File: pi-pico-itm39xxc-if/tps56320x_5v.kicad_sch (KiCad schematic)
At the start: 16 parts

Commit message: Working on pico itm interface
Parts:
- R?: value 30k -> 11k
- R?: value 9k1 -> 2k
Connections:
- net 3V3 renamed 5V
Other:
- note added: "Supply info - Input voltage: 6.7 V - 17 V - Output voltage: 5 V - Output current: 3 A Compatible switching regulators: - TPS56320x - TPS56220x TODO - Make feedback resistors, output capacitors and inductor configurable from the sheet, so that it is possible to obtain any output voltage without changing values inside the sheet."
- note removed: "Supply info - Input voltage: 4.5 V - 17 V - Output voltage: 3.3 V - Output current: 3 A Compatible switching regulators: - TPS56320x - TPS56220x TODO - Make feedback resistors, output capacitors and inductor configurable from the sheet, so that it is possible to obtain any output voltage without changing values inside the sheet."
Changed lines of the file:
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@@
     (stroke (width 0) (type default) (color 0 0 0 0))
   )
-  (text "Supply info\n - Input voltage: 4.5 V - 17 V\n - Output voltage: 3.3 V\n - Output current: 3 A\n\nCompatible switching regulators:\n - TPS56320x\n - TPS56220x\n\nTODO\n - Make feedback resistors, output capacitors and inductor \n configurable from the sheet, so that it is possible to obtain\n any output voltage without changing values inside the sheet."
+  (text "Supply info\n - Input voltage: 6.7 V - 17 V\n - Output voltage: 5 V\n - Output current: 3 A\n\nCompatible switching regulators:\n - TPS56320x\n - TPS56220x\n\nTODO\n - Make feedback resistors, output capacitors and inductor \n configurable from the sheet, so that it is possible to obtain\n any output voltage without changing values inside the sheet."
     (at 14.732 84.328 0)
     (effects (font (size 1.27 1.27)) (justify left bottom))
@@
     (effects (font (size 1.27 1.27)) (justify left bottom))
   )
-  (label "3V3" (at 130.556 22.098 0)
+  (label "5V" (at 130.556 22.098 0)
     (effects (font (size 1.27 1.27)) (justify left bottom))
   )
@@
     (effects (font (size 1.27 1.27)) (justify right bottom))
   )
-  (label "3V3" (at 18.796 45.72 180)
+  (label "5V" (at 18.796 45.72 180)
     (effects (font (size 1.27 1.27)) (justify right bottom))
   )
@@
     (effects (font (size 1.27 1.27)) (justify left))
   )
-  (hierarchical_label "3V3" (shape output) (at 21.336 45.72 0)
+  (hierarchical_label "5V" (shape output) (at 21.336 45.72 0)
     (effects (font (size 1.27 1.27)) (justify left))
   )
@@
       (effects (font (size 1.27 1.27)) (justify left))
     )
-    (property "Value" "30k" (id 1) (at 122.428 29.972 0)
+    (property "Value" "11k" (id 1) (at 122.428 29.972 0)
       (effects (font (size 1.27 1.27)) (justify left))
     )
@@
       (effects (font (size 1.27 1.27)) (justify left))
     )
-    (property "Value" "9k1" (id 1) (at 122.174 36.068 0)
+    (property "Value" "2k" (id 1) (at 122.174 36.068 0)
       (effects (font (size 1.27 1.27)) (justify left))
     )

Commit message: Passing ERC
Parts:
- gave numbers to parts that had none: 16
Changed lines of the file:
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@@
   (symbol (lib_id "Device:C_Small") (at 129.286 28.702 0) (unit 1)
     (in_bom yes) (on_board yes)
-    (property "Reference" "C?" (id 0) (at 131.318 27.432 0)
+    (property "Reference" "C9" (id 0) (at 131.318 27.432 0)
       (effects (font (size 1.27 1.27)) (justify left))
     )
@@
   (symbol (lib_id "Device:R_Small") (at 51.054 27.178 270) (unit 1)
     (in_bom yes) (on_board yes)
-    (property "Reference" "R?" (id 0) (at 51.054 25.4 90))
+    (property "Reference" "R6" (id 0) (at 51.054 25.4 90))
     (property "Value" "10k" (id 1) (at 51.054 28.956 90))
     (property "Footprint" "Resistor_SMD:R_0805_2012Metric_Pad1.20x1.40mm_HandSolder" (id 2) (at 51.054 27.178 0)
@@
   (symbol (lib_id "Device:R_Small") (at 121.158 28.702 0) (unit 1)
     (in_bom yes) (on_board yes)
-    (property "Reference" "R?" (id 0) (at 122.174 27.432 0)
+    (property "Reference" "R7" (id 0) (at 122.174 27.432 0)
       (effects (font (size 1.27 1.27)) (justify left))
     )
@@
   (symbol (lib_id "Device:C_Small") (at 102.87 25.908 0) (unit 1)
     (in_bom yes) (on_board yes)
-    (property "Reference" "C?" (id 0) (at 104.902 24.638 0)
+    (property "Reference" "C7" (id 0) (at 104.902 24.638 0)
       (effects (font (size 1.27 1.27)) (justify left))
     )
@@
   (symbol (lib_id "Device:C_Small") (at 29.464 25.908 0) (unit 1)
     (in_bom yes) (on_board yes)
-    (property "Reference" "C?" (id 0) (at 31.496 24.638 0)
+    (property "Reference" "C4" (id 0) (at 31.496 24.638 0)
       (effects (font (size 1.27 1.27)) (justify left))
     )
@@
   (symbol (lib_id "Device:C_Small") (at 20.32 25.908 0) (unit 1)
     (in_bom yes) (on_board yes)
-    (property "Reference" "C?" (id 0) (at 22.352 24.638 0)
+    (property "Reference" "C3" (id 0) (at 22.352 24.638 0)
       (effects (font (size 1.27 1.27)) (justify left))
     )
@@
   (symbol (lib_id "Connector:TestPoint_Small") (at 80.01 19.304 0) (unit 1)
     (in_bom yes) (on_board yes)
-    (property "Reference" "TP?" (id 0) (at 80.518 19.304 0)
+    (property "Reference" "TP1" (id 0) (at 80.518 19.304 0)
       (effects (font (size 1.27 1.27)) (justify left))
     )
@@
   (symbol (lib_id "Device:C_Small") (at 38.608 25.908 0) (unit 1)
     (in_bom yes) (on_board yes)
-    (property "Reference" "C?" (id 0) (at 40.64 24.638 0)
+    (property "Reference" "C5" (id 0) (at 40.64 24.638 0)
       (effects (font (size 1.27 1.27)) (justify left))
     )
@@
   (symbol (lib_id "Device:R_Small") (at 121.158 34.798 0) (unit 1)
     (in_bom yes) (on_board yes)
-    (property "Reference" "R?" (id 0) (at 122.174 33.528 0)
+    (property "Reference" "R8" (id 0) (at 122.174 33.528 0)
       (effects (font (size 1.27 1.27)) (justify left))
     )
@@
   (symbol (lib_id "CL_Regulator_Switching:TPS56320x") (at 65.024 24.638 0) (unit 1)
     (in_bom yes) (on_board yes)
-    (property "Reference" "U?" (id 0) (at 58.42 18.288 0))
+    (property "Reference" "U2" (id 0) (at 58.42 18.288 0))
     (property "Value" "TPS56320x" (id 1) (at 67.31 18.542 0))
     (property "Footprint" "Package_TO_SOT_SMD:SOT-23-6" (id 2) (at 66.294 30.988 0)
@@
   (symbol (lib_id "Device:C_Small") (at 93.726 25.908 0) (unit 1)
     (in_bom yes) (on_board yes)
-    (property "Reference" "C?" (id 0) (at 95.758 24.638 0)
+    (property "Reference" "C6" (id 0) (at 95.758 24.638 0)
       (effects (font (size 1.27 1.27)) (justify left))
     )
@@
   (symbol (lib_id "Device:C_Small") (at 112.014 25.908 0) (unit 1)
     (in_bom yes) (on_board yes)
-    (property "Reference" "C?" (id 0) (at 114.046 24.638 0)
+    (property "Reference" "C8" (id 0) (at 114.046 24.638 0)
       (effects (font (size 1.27 1.27)) (justify left))
     )
@@
   (symbol (lib_id "Connector:TestPoint_Small") (at 102.87 19.304 0) (unit 1)
     (in_bom yes) (on_board yes)
-    (property "Reference" "TP?" (id 0) (at 103.378 19.304 0)
+    (property "Reference" "TP2" (id 0) (at 103.378 19.304 0)
       (effects (font (size 1.27 1.27)) (justify left))
     )
@@
   (symbol (lib_id "Device:C_Small") (at 82.296 24.638 270) (unit 1)
     (in_bom yes) (on_board yes)
-    (property "Reference" "C?" (id 0) (at 78.994 23.622 90)
+    (property "Reference" "C2" (id 0) (at 78.994 23.622 90)
       (effects (font (size 1.27 1.27)) (justify left))
     )
@@
   (symbol (lib_id "Device:L_Small") (at 89.916 22.098 90) (unit 1)
     (in_bom yes) (on_board yes)
-    (property "Reference" "L?" (id 0) (at 89.916 18.288 90))
+    (property "Reference" "L1" (id 0) (at 89.916 18.288 90))
     (property "Value" "4.7uH" (id 1) (at 89.916 20.32 90))
     (property "Footprint" "Inductor_SMD:L_Bourns_SRP7028A_7.3x6.6mm" (id 2) (at 89.916 22.098 0)
@@
   (symbol (lib_id "Connector:TestPoint_Small") (at 75.946 29.21 0) (unit 1)
     (in_bom yes) (on_board yes)
-    (property "Reference" "TP?" (id 0) (at 74.422 30.734 0)
-      (effects (font (size 1.27 1.27)) (justify left))
-    )
+    (property "Reference" "TP3" (id 0) (at 74.422 30.734 0)
+      (effects (font (size 1.27 1.27)) (justify left))
+    )

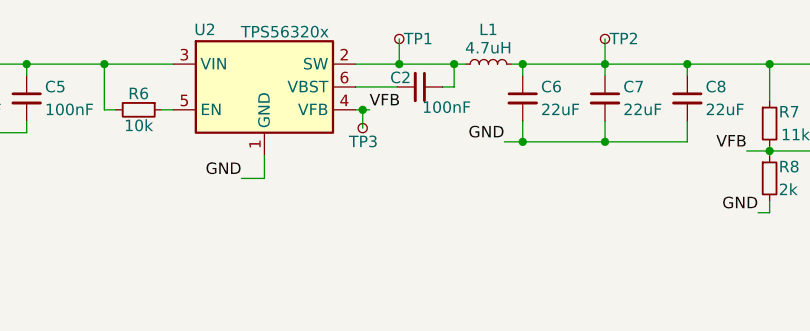
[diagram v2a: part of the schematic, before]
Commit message: Working on pcb for pi pico it
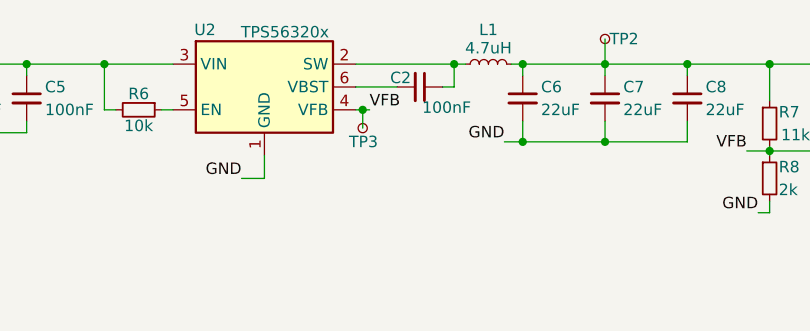
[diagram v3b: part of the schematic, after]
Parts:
- removed TP1: TestPoint_Small, TestPoint:TestPoint_Pad_2.0x2.0mm, symbol Connector:TestPoint_Small
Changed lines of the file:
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@@
   (junction (at 29.464 22.098) (diameter 0) (color 0 0 0 0)
   )
-  (junction (at 80.01 22.098) (diameter 0) (color 0 0 0 0)
-  )
   (junction (at 38.608 22.098) (diameter 0) (color 0 0 0 0)
   )
@@
     (stroke (width 0) (type default) (color 0 0 0 0))
   )
-  (wire (pts (xy 75.184 22.098) (xy 80.01 22.098))
+  (wire (pts (xy 75.184 22.098) (xy 86.106 22.098))
     (stroke (width 0) (type default) (color 0 0 0 0))
   )
@@
     (stroke (width 0) (type default) (color 0 0 0 0))
   )
-  (wire (pts (xy 80.01 22.098) (xy 86.106 22.098))
-    (stroke (width 0) (type default) (color 0 0 0 0))
-  )
   (wire (pts (xy 102.87 30.734) (xy 93.726 30.734))
     (stroke (width 0) (type default) (color 0 0 0 0))
@@
   )
   (wire (pts (xy 121.158 31.242) (xy 121.158 31.75))
-    (stroke (width 0) (type default) (color 0 0 0 0))
-  )
-  (wire (pts (xy 80.01 19.304) (xy 80.01 22.098))
     (stroke (width 0) (type default) (color 0 0 0 0))
   )
@@
     (pin "2")
   )
-  (symbol (lib_id "Connector:TestPoint_Small") (at 80.01 19.304 0) (unit 1)
-    (in_bom yes) (on_board yes)
-    (property "Reference" "TP1" (id 0) (at 80.518 19.304 0)
-      (effects (font (size 1.27 1.27)) (justify left))
-    )
-    (property "Value" "TestPoint_Small" (id 1) (at 81.534 20.5739 0)
-      (effects (font (size 1.27 1.27)) (justify left) hide)
-    )
-    (property "Footprint" "TestPoint:TestPoint_Pad_2.0x2.0mm" (id 2) (at 85.09 19.304 0)
-      (effects (font (size 1.27 1.27)) hide)
-    )
-    (property "Datasheet" "~" (id 3) (at 85.09 19.304 0)
-      (effects (font (size 1.27 1.27)) hide)
-    )
-    (pin "1")
-  )
   (symbol (lib_id "Device:C_Small") (at 38.608 25.908 0) (unit 1)
